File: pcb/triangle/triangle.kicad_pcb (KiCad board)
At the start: 2 copper layers, 52 x 60.3 mm, 65 parts, among them J1 Conn_01x03_Male, J2 Conn_01x03_Male

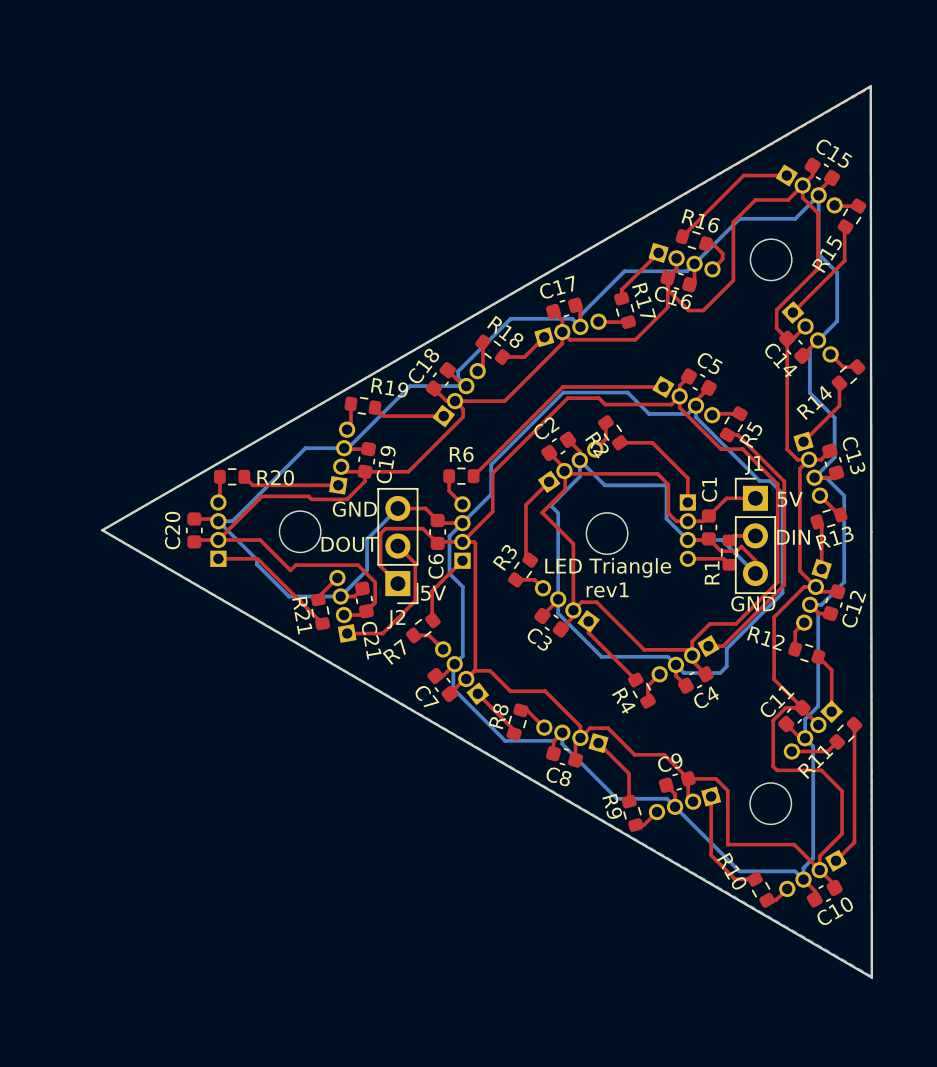
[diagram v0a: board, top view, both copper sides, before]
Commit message: Split PCB one large PCB gap into 2 smaller gaps.
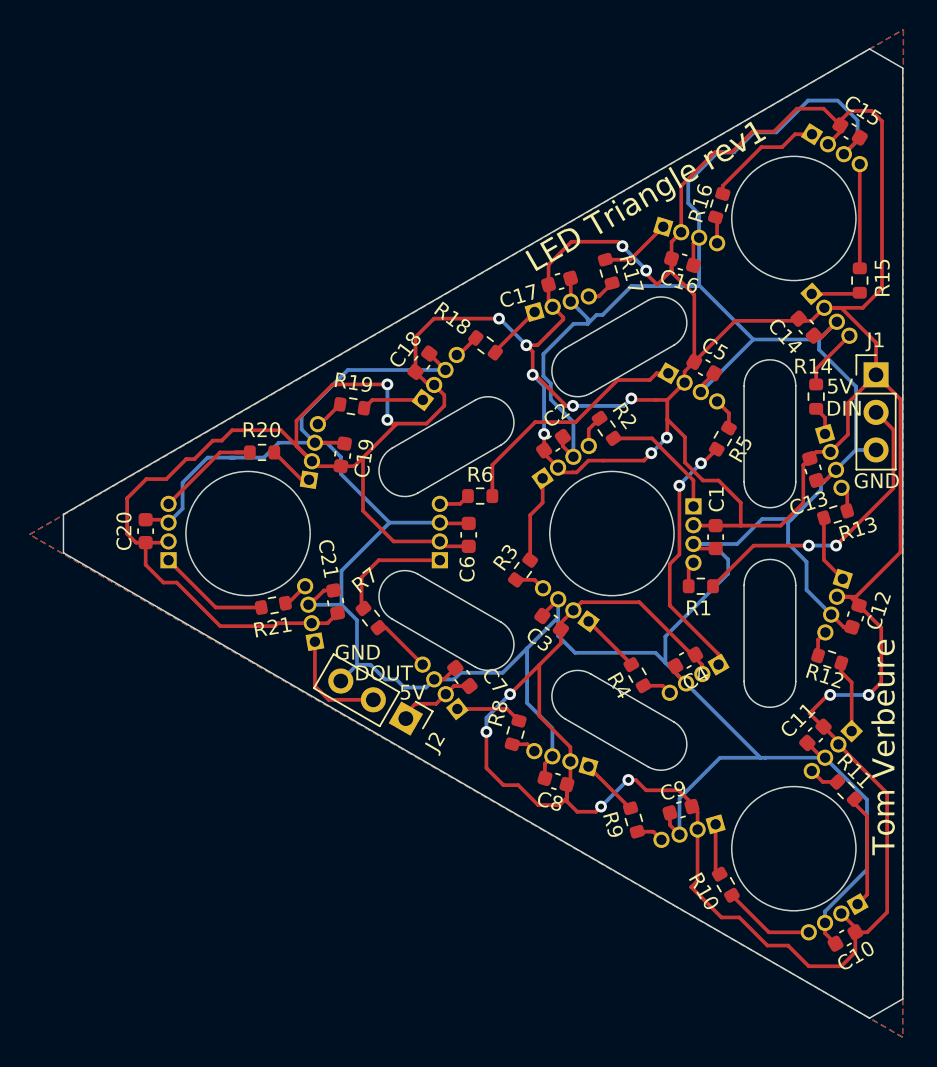
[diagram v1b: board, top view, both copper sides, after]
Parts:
- moved J1 11.7 mm to (160.1, 72.9)
- moved J2 9.15 mm to (128.2, 96.2), turned to -120 degrees
- moved R15 4.37 mm to (158.9, 66.5), turned to -90 degrees
- moved R11 3.88 mm to (158.0, 101.0), turned to -45 degrees
- moved R7 3.60 mm to (125.9, 89.3), turned to 128 degrees
- moved D20 3.37 mm to (112.2, 83.5)
- moved C15 3.32 mm to (158.3, 56.4)
- moved C10 3.31 mm to (158.0, 111.0)
- moved C20 3.29 mm to (110.7, 83.5)
- moved D10 3.28 mm to (157.2, 109.7)
- moved D15 3.27 mm to (157.3, 57.6)
- moved R21 3.22 mm to (119.3, 88.5), turned to -170 degrees
- moved R1 2.99 mm to (148.2, 87.2), turned to 0 degrees
- moved R16 2.89 mm to (149.4, 61.5), turned to 73 degrees
- moved R17 2.86 mm to (142.0, 65.9)
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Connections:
- net Net-(D21-Pad1) renamed /DOUT
- net Net-(J1-Pad2) renamed /DIN
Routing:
- net +5V: track 296.9 -> 364.6 mm, vias 0 -> 18
- net GND: track 291.5 -> 266.2 mm
- net /DIN: track 1.88 -> 20.6 mm, vias 0 -> 2
- net Net-(D20-Pad4): track 1.78 -> 7.94 mm
- net Net-(D15-Pad4): track 1.64 -> 7.05 mm
- net Net-(D10-Pad4): track 1.67 -> 6.24 mm
- net Net-(D9-Pad1): track 7.61 -> 3.48 mm
- net Net-(D14-Pad1): track 7.27 -> 3.28 mm
- net Net-(D19-Pad1): track 6.59 -> 3.12 mm
- net Net-(D6-Pad1): track 4.91 -> 8.08 mm
- net Net-(D13-Pad1): track 4.96 -> 1.95 mm
- net /DOUT: track 9.72 -> 7.34 mm
- net Net-(D14-Pad4): track 2.18 -> 4.23 mm
- net Net-(D10-Pad1): track 9.72 -> 7.72 mm
- net Net-(D4-Pad1): track 19.0 -> 17.3 mm, vias 0 -> 2
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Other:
- board size 52 x 60.3 mm -> 56.8 x 65.5 mm
- board text added: "Tom Verbeure"

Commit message: Triangle PCB v2.
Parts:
- moved R2 0.41 mm to (142.2, 76.4)
- moved C1 0.40 mm to (149.6, 83.9)
- moved C4 0.39 mm to (146.9, 91.9)
- moved R1 0.35 mm to (148.2, 87.5)
- moved R6 0.35 mm to (133.3, 81.5)
- moved C5 0.32 mm to (148.5, 72.1)
- moved C2 0.31 mm to (138.1, 77.3)
- moved C7 0.30 mm to (132.1, 93.6)
- moved D13 0.28 mm to (157.4, 78.6)
- moved C3 0.26 mm to (137.9, 89.9)
- moved C15 0.26 mm to (158.4, 56.2)
- moved C13 0.25 mm to (156.1, 79.2)
- moved C9 0.25 mm to (146.8, 102.1)
- moved D7 0.24 mm to (130.4, 94.1)
- moved R21 0.23 mm to (119.1, 88.5)
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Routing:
- net +5V: track 364.6 -> 448.5 mm
- net GND: track 266.2 -> 276.0 mm
- net /DIN: track 20.6 -> 21.8 mm
- net Net-(D12-Pad1): track 4.65 -> 5.19 mm
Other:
- board text added: "LED Triangle rev2"
- board text removed: "LED Triangle rev1"

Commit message: LED & battery holder fixes.
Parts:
- moved D1 0.13 mm to (147.8, 83.7)
- moved R5 0.11 mm to (149.6, 77.2)
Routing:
- net +5V: track 448.5 -> 459.2 mm
- net GND: track 276.0 -> 278.9 mm
- net Net-(D14-Pad1): track 3.28 -> 3.85 mm
